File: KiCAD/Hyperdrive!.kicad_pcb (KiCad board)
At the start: 2 copper layers, 72 x 64 mm, 79 parts, among them CON1 USB-MINI-B, K1 SPRI/O, P1 RIR PCB, P2 ICSP, P3 Display PCB, P4 Motor Feedback PCB, P5 Extra I/Os, P6 EDG_SEN, P7 PWR, U1 24AA256, U2 LD39200, U3 LT3464, U4 DSPIC33EP512GM706, U5 FT201X, U6 GP2Y0A51SK0F, U7 LSM330, U8 GP2Y0E03, X1 16MHz

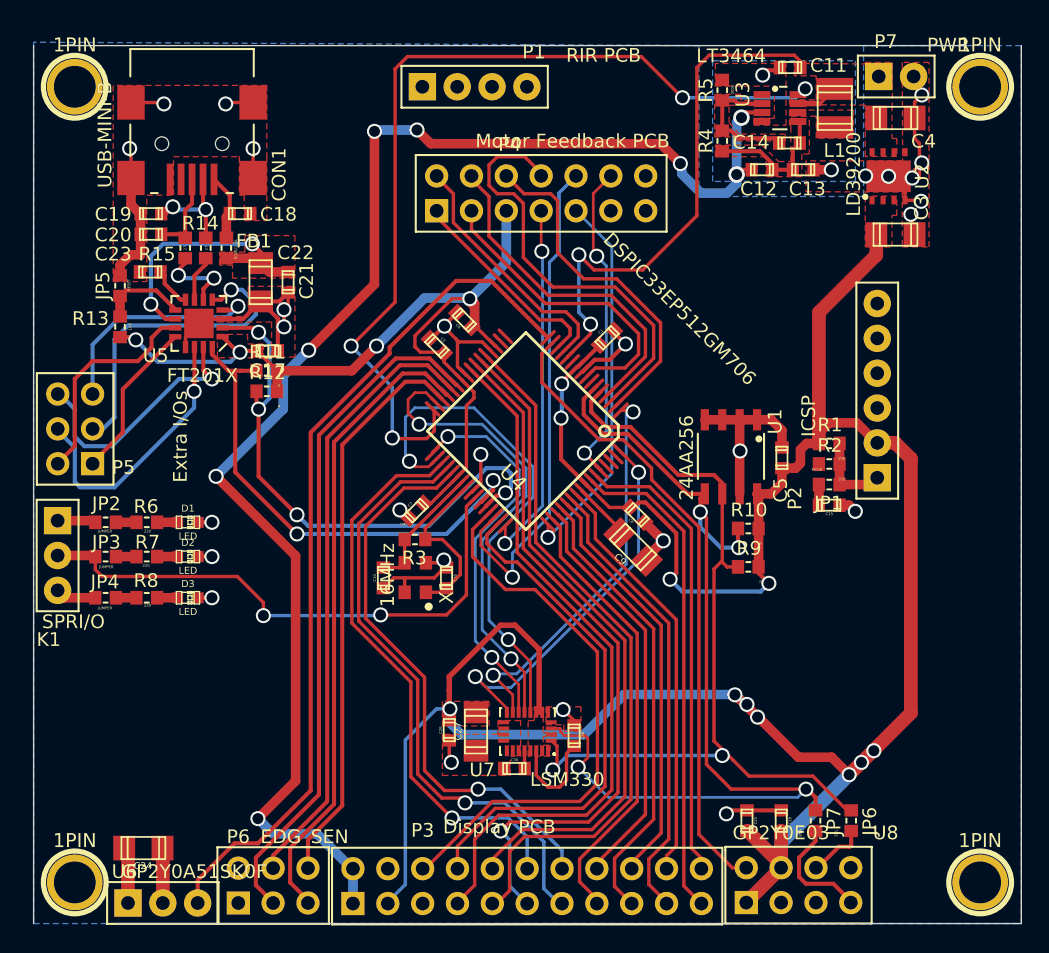
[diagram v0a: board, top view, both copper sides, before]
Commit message: Updated 3D-Model, and finished main PCB
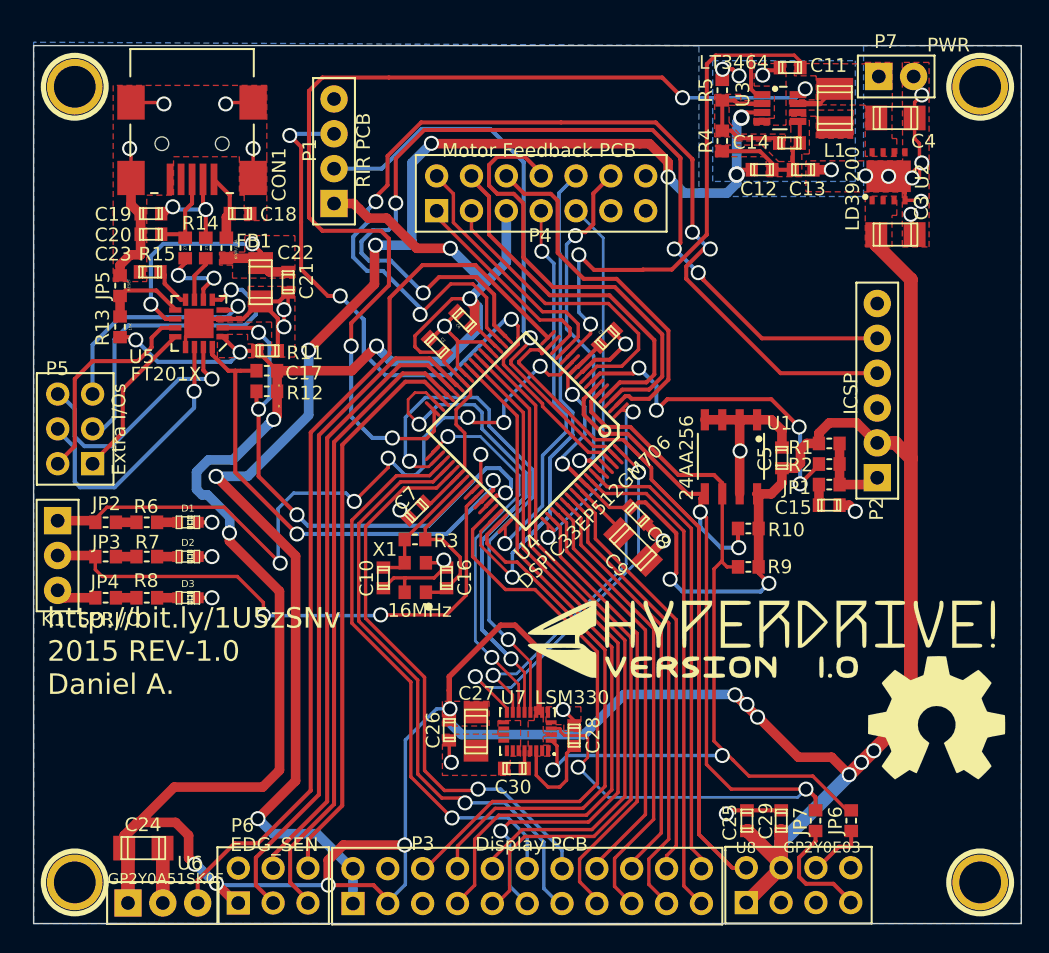
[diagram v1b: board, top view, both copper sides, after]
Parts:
- added G***: OSHW-logo_silkscreen-front_10mm, OSHW-logo_silkscreen-front_10mm, F.Cu at (168.8, 109.0)
- added VAL: REF, Hyperdrive!_F.SilkS_40mm, F.Cu at (155.9, 103.3)
- ? (x4): renamed from 1PIN; value P*** -> (none)
- CON1: value USB-MINI-B -> (none)
- JP2, JP3, JP4: value JUMPER -> (none)
- moved P1 16.7 mm to (124.9, 61.4), turned to 90 degrees
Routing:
- net +3.3V: track 272.8 -> 373.5 mm, vias 15 -> 22
- net /PGD: track 0.00 -> 76.6 mm, vias 0 -> 4
- net /Sensors /IMU_INT1_G: track 34.3 -> 105.3 mm
- net /PGC: track 0.00 -> 70.7 mm, vias 0 -> 4
- net /IRPWM: track 0.00 -> 52.4 mm, vias 0 -> 3
- net /I/O1: track 2.80 -> 53.4 mm, vias 0 -> 6
- net /IRBDS: track 0.00 -> 42.0 mm, vias 0 -> 1
- net /Sensors /IRLDS_VO: track 46.4 -> 84.4 mm
- net N-000005: track 0.00 -> 25.2 mm, vias 0 -> 4
- net /PWML: track 31.6 -> 49.3 mm
- net /PWMR: track 25.3 -> 38.6 mm
- net /SHDN: track 66.9 -> 76.6 mm
- net +BATT: track 41.9 -> 49.8 mm
- net /Sensors /IMU_INT2_G: track 37.6 -> 42.9 mm
- net /VDD2: track 25.2 -> 28.5 mm
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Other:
- outline, holes or cut-outs redrawn
- board text added: "http://bit.ly/1U5zSNv 2015 REV-1.0 Daniel A."

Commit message: Updated 3D-Model, and PCBs.
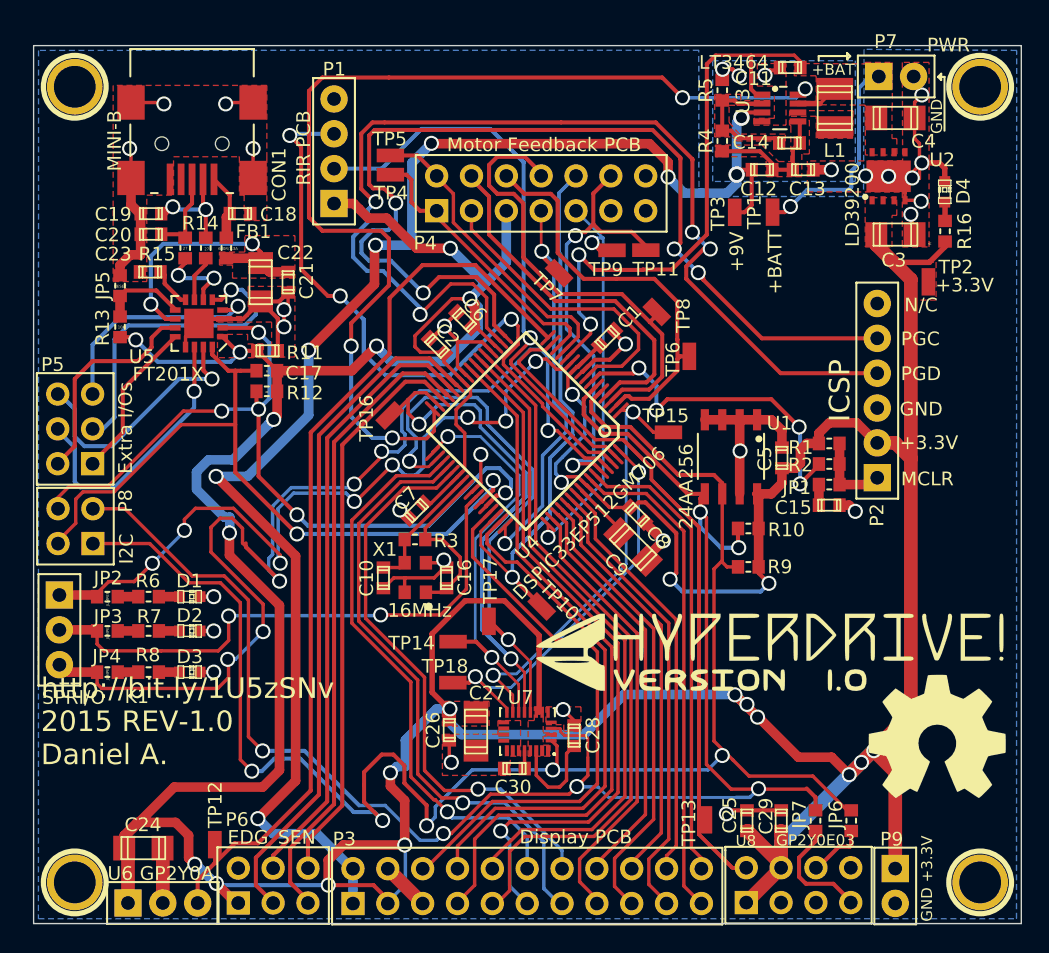
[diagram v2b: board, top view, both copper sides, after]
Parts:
- added D4: , LED-0603, F.Cu at (169.4, 70.7)
- added P8: , CON_2x2, F.Cu at (104.8, 93.8)
- added P9: , CON_2x1, F.Cu at (165.8, 122.5)
- added R16: R, r_0603, F.Cu at (169.4, 73.5)
- added TP1: , TP, F.Cu at (156.9, 72.1)
- added TP10: , TP, F.Cu at (140.0, 100.9)
- added TP11: , TP, F.Cu at (147.6, 74.9)
- added TP12: , TP, F.Cu at (116.2, 118.2)
- added TP13: , TP, F.Cu at (152.0, 116.4)
- added TP14: , TP, F.Cu at (133.6, 103.5)
- added TP15: , TP, F.Cu at (149.3, 88.2)
- added TP16: , TP, F.Cu at (129.0, 87.0)
- added TP17: , TP, F.Cu at (136.2, 102.0)
- added TP18: , TP, F.Cu at (133.6, 106.4)
- added TP2: , TP, F.Cu at (168.2, 77.2)
- added TP3: , TP, F.Cu at (154.1, 72.2)
- added TP4: , TP, F.Cu at (129.0, 69.4)
- added TP5: , TP, F.Cu at (129.0, 68.0)
- added TP6: , TP, F.Cu at (150.8, 82.7)
- added TP7: , TP, F.Cu at (141.3, 76.6)
- added TP8: , TP, F.Cu at (148.4, 79.4)
- added TP9: , TP, F.Cu at (145.2, 74.9)
- D1, D2, D3: value LED -> (none)
- JP2, JP3, JP4: value (none) -> JUMPER
- K1: value SPRI/O -> (none)
- P1: value RIR PCB -> (none)
- P2: value ICSP -> (none)
- P3: value Display PCB -> (none)
- P4: value Motor Feedback PCB -> (none)
- P5: value Extra I/Os -> (none)
- P6: value EDG_SEN -> (none)
- U6: value GP2Y0A51SK0F -> (none)
- U7: value LSM330 -> (none)
- U8: value GP2Y0E03 -> (none)
- moved D1 5.42 mm to (114.4, 100.2)
- moved D2 5.42 mm to (114.4, 102.7)
- moved D3 5.42 mm to (114.4, 105.7)
- moved JP2 5.42 mm to (108.4, 100.2)
- moved JP3 5.42 mm to (108.4, 102.7)
- moved JP4 5.42 mm to (108.4, 105.7)
- moved K1 5.42 mm to (104.9, 107.7)
- moved R6 5.42 mm to (111.4, 100.2)
- moved R7 5.42 mm to (111.4, 102.7)
- moved R8 5.42 mm to (111.4, 105.7)
- moved G*** 1.36 mm to (168.9, 110.4)
- moved VAL 1.13 mm to (156.5, 104.2)
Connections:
- U4 pad 61: (no net) -> /I/03
- X1 pad 3: (no net) -> GND
- X1 pad 4: (no net) -> GND
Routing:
- net /I/03: track 2.97 -> 83.2 mm, vias 0 -> 6
- net /Sensors /IMU_SCL: track 61.7 -> 122.9 mm, vias 2 -> 5
- net /Sensors /IMU_SDA: track 72.9 -> 124.2 mm, vias 4 -> 6
- net +3.3V: track 373.5 -> 395.9 mm, vias 22 -> 23
- net /SDA/FM+: track 40.2 -> 58.4 mm, vias 4 -> 5
- net /SCL/FM+: track 36.2 -> 53.8 mm
- net +BATT: track 49.8 -> 65.6 mm, vias 2 -> 3
- net GND: track 122.3 -> 128.6 mm
- net /FAULTL: track 25.9 -> 31.8 mm
- net /Sensors /IMU_INT1_G: track 105.3 -> 110.7 mm
- net /MSL: track 15.3 -> 20.7 mm
- net /PGC: track 70.7 -> 74.9 mm
- net /MSR: track 18.6 -> 22.6 mm
- net +9V: track 105.6 -> 109.7 mm
- net /Sensors /IMU_INT1_A: track 28.0 -> 31.3 mm
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- added copper zone on F.Cu, net N-0000060
- removed copper zone on F.Cu, net N-0000025
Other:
- net class Default: trace_width 0.2032 -> 0.1524
- rule trace_min: 0.2032 -> 0.1524
- board text added: "+3.3V"
- board text added: "+9V"
- board text added: "+BAT"
- board text added: "+BATT"
- board text added: "Display PCB"
- board text added: "EDG_SEN"
- board text added: "Extra I/Os"
- board text added: "GND"
- board text added: "GP2Y0A"
- board text added: "GP2Y0E03"
- board text added: "I2C"
- board text added: "ICSP"
- board text added: "MCLR"
- board text added: "MINI-B"
- board text added: "Motor Feedback PCB"
- board text added: "N/C"
- board text added: "PGC"
- board text added: "PGD"
- board text added: "RIR PCB"
- board text added: "SPRI/O"
